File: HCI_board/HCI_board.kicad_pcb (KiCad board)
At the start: 2 copper layers, 30 x 68 mm, 28 parts, among them J1 MCU Controls, J3 Power, J4 USB Data, J7 DC Motor Terminal, J9 USBC_RECP, SW1 Trigger, SW2 Increment, SW3 Reset, SW4 Decrement, U1 NCP1117, U3 DRV8833PWP

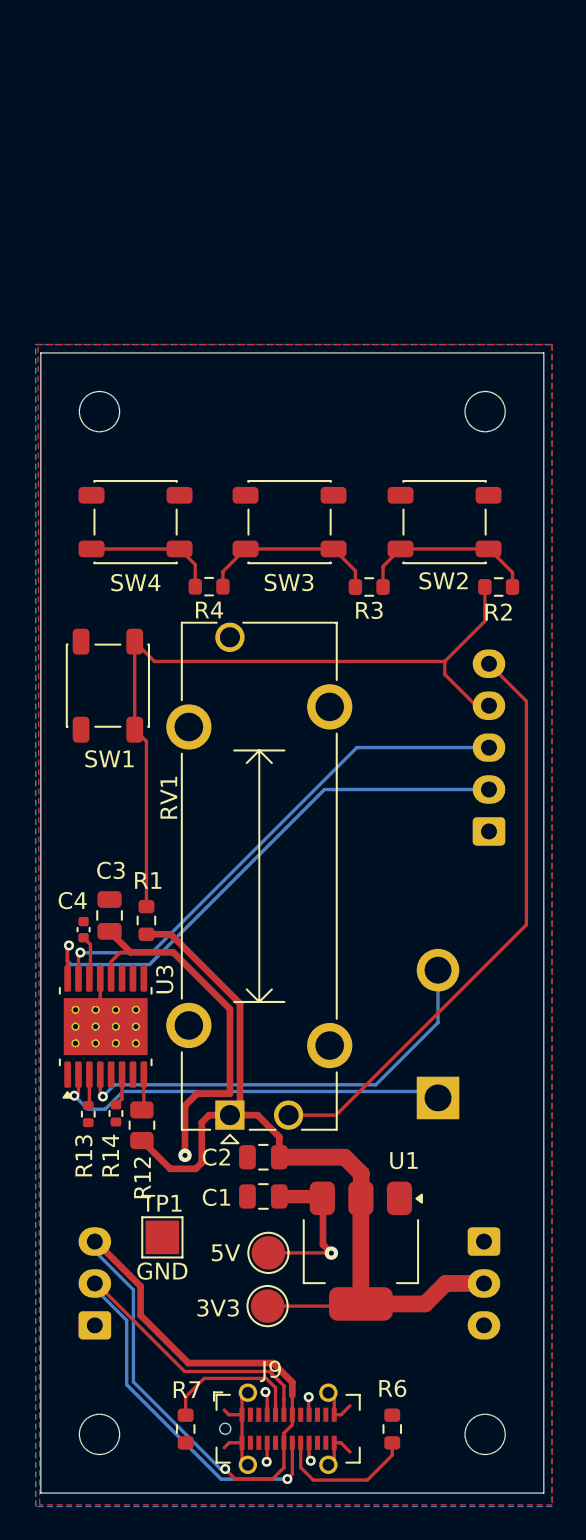
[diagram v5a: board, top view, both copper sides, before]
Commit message: Replaced connectors with Clik-Mate Reorganized traces Set planes to both be ground and rerouted power Moved motor driver Organized buttons & slide pot
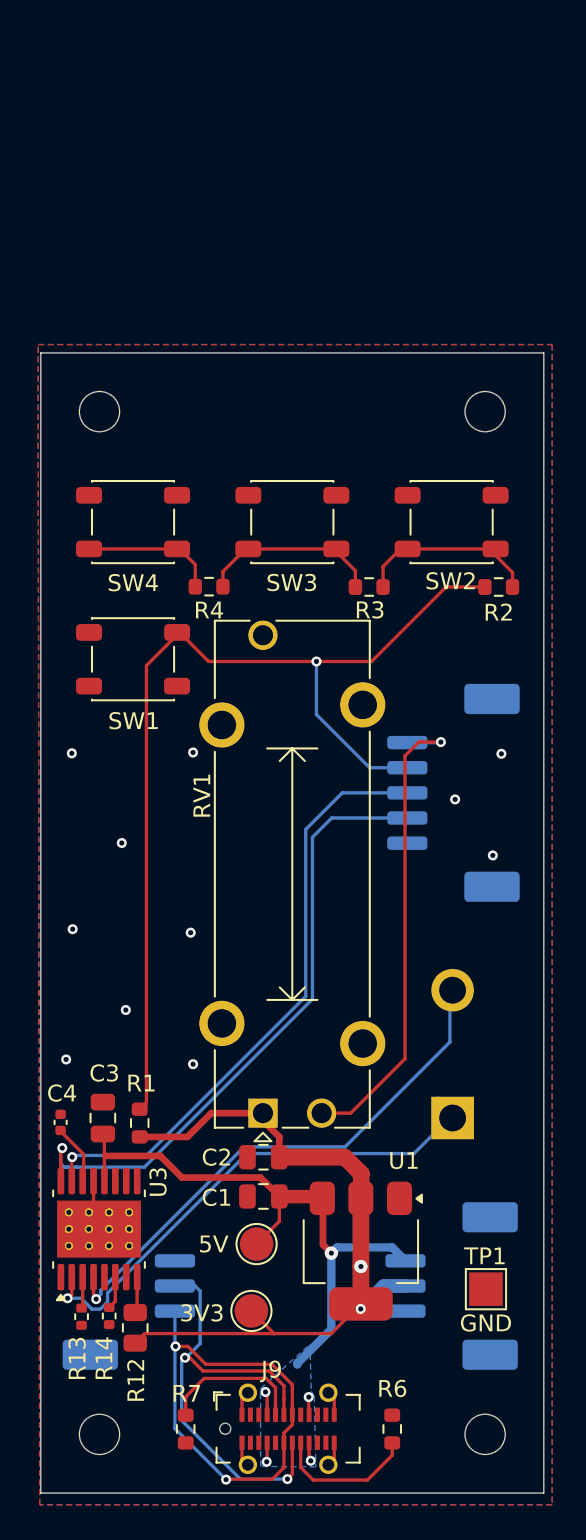
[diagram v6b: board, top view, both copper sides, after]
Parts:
- J1: footprint Connector_JST:JST_EH_B5B-EH-A_1x05_P2.50mm_Vertical -> Connector_Molex:Molex_CLIK-Mate_505405-0570_1x05-1MP_P1.50mm_Vertical
- J3, J4: footprint Connector_JST:JST_EH_B3B-EH-A_1x03_P2.50mm_Vertical -> Connector_Molex:Molex_CLIK-Mate_505405-0370_1x03-1MP_P1.50mm_Vertical
- moved TP1 19.5 mm to (146.6, 135.8)
- moved R1 12.1 mm to (125.9, 125.9)
- moved R12 12.1 mm to (125.6, 138.1)
- moved C3 12.1 mm to (123.7, 125.6)
- moved R14 12.1 mm to (124.1, 137.4)
- moved U3 12.1 mm to (123.5, 132.3)
- moved R13 12.1 mm to (122.4, 137.5)
- moved C4 11.6 mm to (121.2, 125.9)
- moved J3 3.28 mm to (144.5, 135.7), turned to 90 degrees
- moved J1 3.13 mm to (144.6, 106.2)
- moved J4 3.11 mm to (125.2, 135.7), turned to -90 degrees
- moved SW1 2.18 mm to (125.5, 98.3), turned to 0 degrees
- moved RV1 1.97 mm to (133.2, 125.3)
- moved J7 1.48 mm to (144.6, 125.6)
- moved TP3 1.01 mm to (132.6, 137.1)
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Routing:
- net /BTN: track 44.7 -> 60.1 mm, vias 0 -> 1
- net /USB D-: track 42.7 -> 28.4 mm, vias 1 -> 2
- net /USB D+: track 36.7 -> 28.2 mm, vias 1 -> 2
- net +3.3V: track 54.5 -> 46.2 mm, vias 0 -> 2
- net /POT: track 35.4 -> 29.0 mm, vias 0 -> 1
- net GND: track 15.8 -> 9.42 mm, vias 0 -> 11
- net Net-(J7-Pin_2): track 26.3 -> 32.1 mm
- net Net-(J7-Pin_1): track 24.1 -> 29.6 mm
- net /AIN2: track 31.0 -> 36.3 mm
- net /AIN1: track 32.8 -> 38.0 mm
- net +5V: track 37.4 -> 41.7 mm, vias 6 -> 5
- net Net-(U3-VINT): track 2.63 -> 3.62 mm
- added copper zone on B.Cu, net GND

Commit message: Updated connectors to consolidate
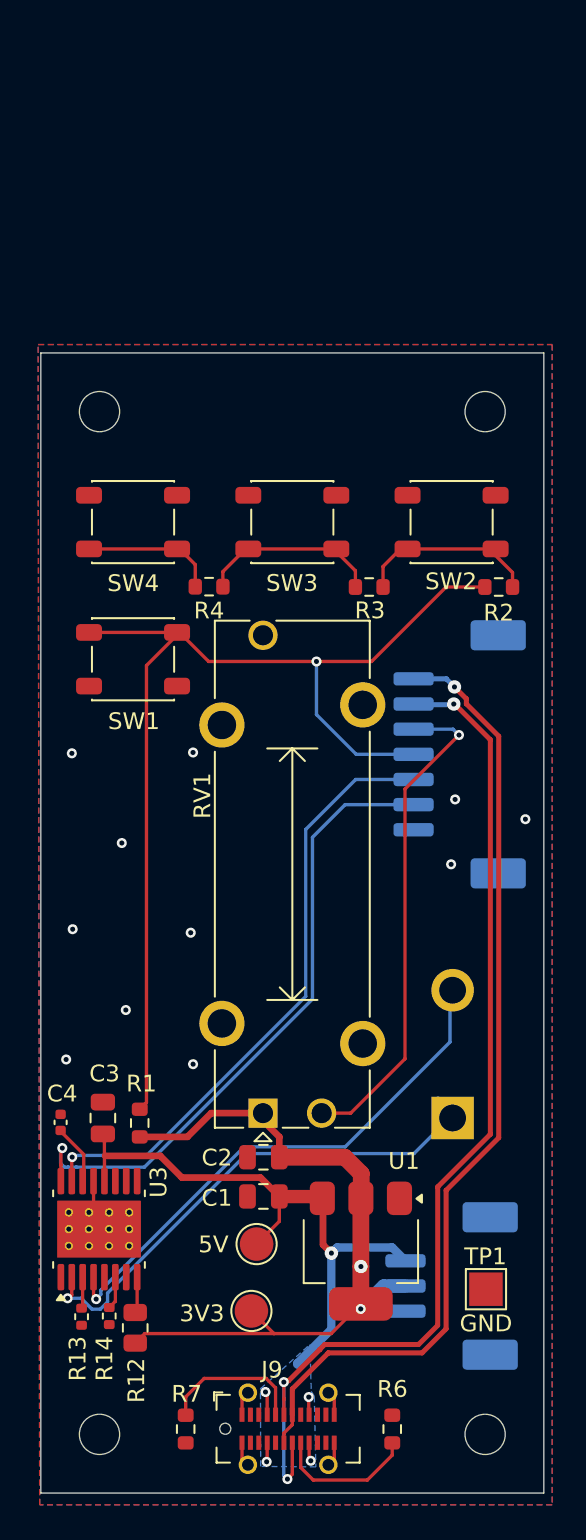
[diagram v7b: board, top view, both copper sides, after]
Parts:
- removed J4: USB Data, Connector_Molex:Molex_CLIK-Mate_505405-0370_1x03-1MP_P1.50mm_Vertical
- J1: footprint Connector_Molex:Molex_CLIK-Mate_505405-0570_1x05-1MP_P1.50mm_Vertical -> Connector_Molex:Molex_CLIK-Mate_505405-0770_1x07-1MP_P1.50mm_Vertical
- moved J1 2.33 mm to (145.0, 103.9)
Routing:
- net /USB D+: track 28.2 -> 62.5 mm, vias 2 -> 3
- net /USB D-: track 28.4 -> 57.5 mm, vias 2 -> 1
- net /BTN: track 60.1 -> 65.4 mm
- net /POT: track 29.0 -> 29.9 mm
- net /AIN2: track 36.3 -> 37.0 mm
- net /AIN1: track 38.0 -> 38.7 mm

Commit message: Rearranged buttons, shrunk bored, changed test points
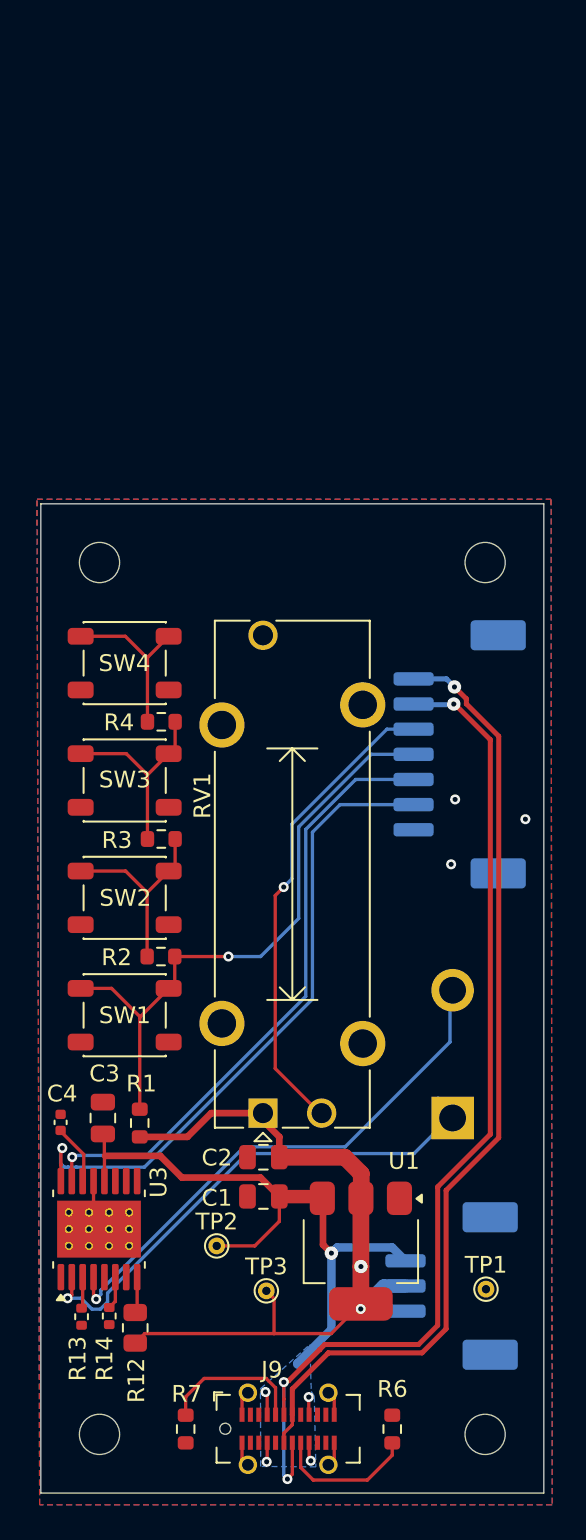
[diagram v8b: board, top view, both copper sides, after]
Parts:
- TP1: footprint TestPoint:TestPoint_Pad_2.0x2.0mm -> TestPoint:TestPoint_THTPad_D1.0mm_Drill0.5mm
- TP2, TP3: footprint TestPoint:TestPoint_Pad_D2.0mm -> TestPoint:TestPoint_THTPad_D1.0mm_Drill0.5mm
- moved R2 29.9 mm to (127.2, 116.0), turned to 180 degrees
- moved SW2 29.7 mm to (125.0, 112.5), turned to 0 degrees
- moved SW1 21.2 mm to (125.0, 119.5)
- moved R3 19.5 mm to (127.2, 109.0)
- moved SW3 18.4 mm to (125.0, 105.5), turned to 0 degrees
- moved R4 8.55 mm to (127.2, 102.0)
- moved SW4 8.42 mm to (125.0, 98.5), turned to 0 degrees
- moved TP2 2.38 mm to (130.5, 133.3)
- moved TP3 1.49 mm to (133.4, 135.9)
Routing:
- net /BTN: track 65.4 -> 36.7 mm
- net +5V: track 41.7 -> 44.2 mm
- net Net-(R4-Pad2): track 7.89 -> 10.1 mm
- net /POT: track 29.9 -> 28.3 mm
- net Net-(R3-Pad2): track 10.9 -> 12.2 mm
- net Net-(R2-Pad2): track 11.1 -> 12.2 mm
- net +3.3V: track 46.2 -> 47.0 mm
- net GND: vias 11 -> 3
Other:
- board size 30 x 68 mm -> 30 x 59 mm
